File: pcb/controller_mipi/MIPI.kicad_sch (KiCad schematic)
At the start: 4 parts, among them J1 1-84952-5

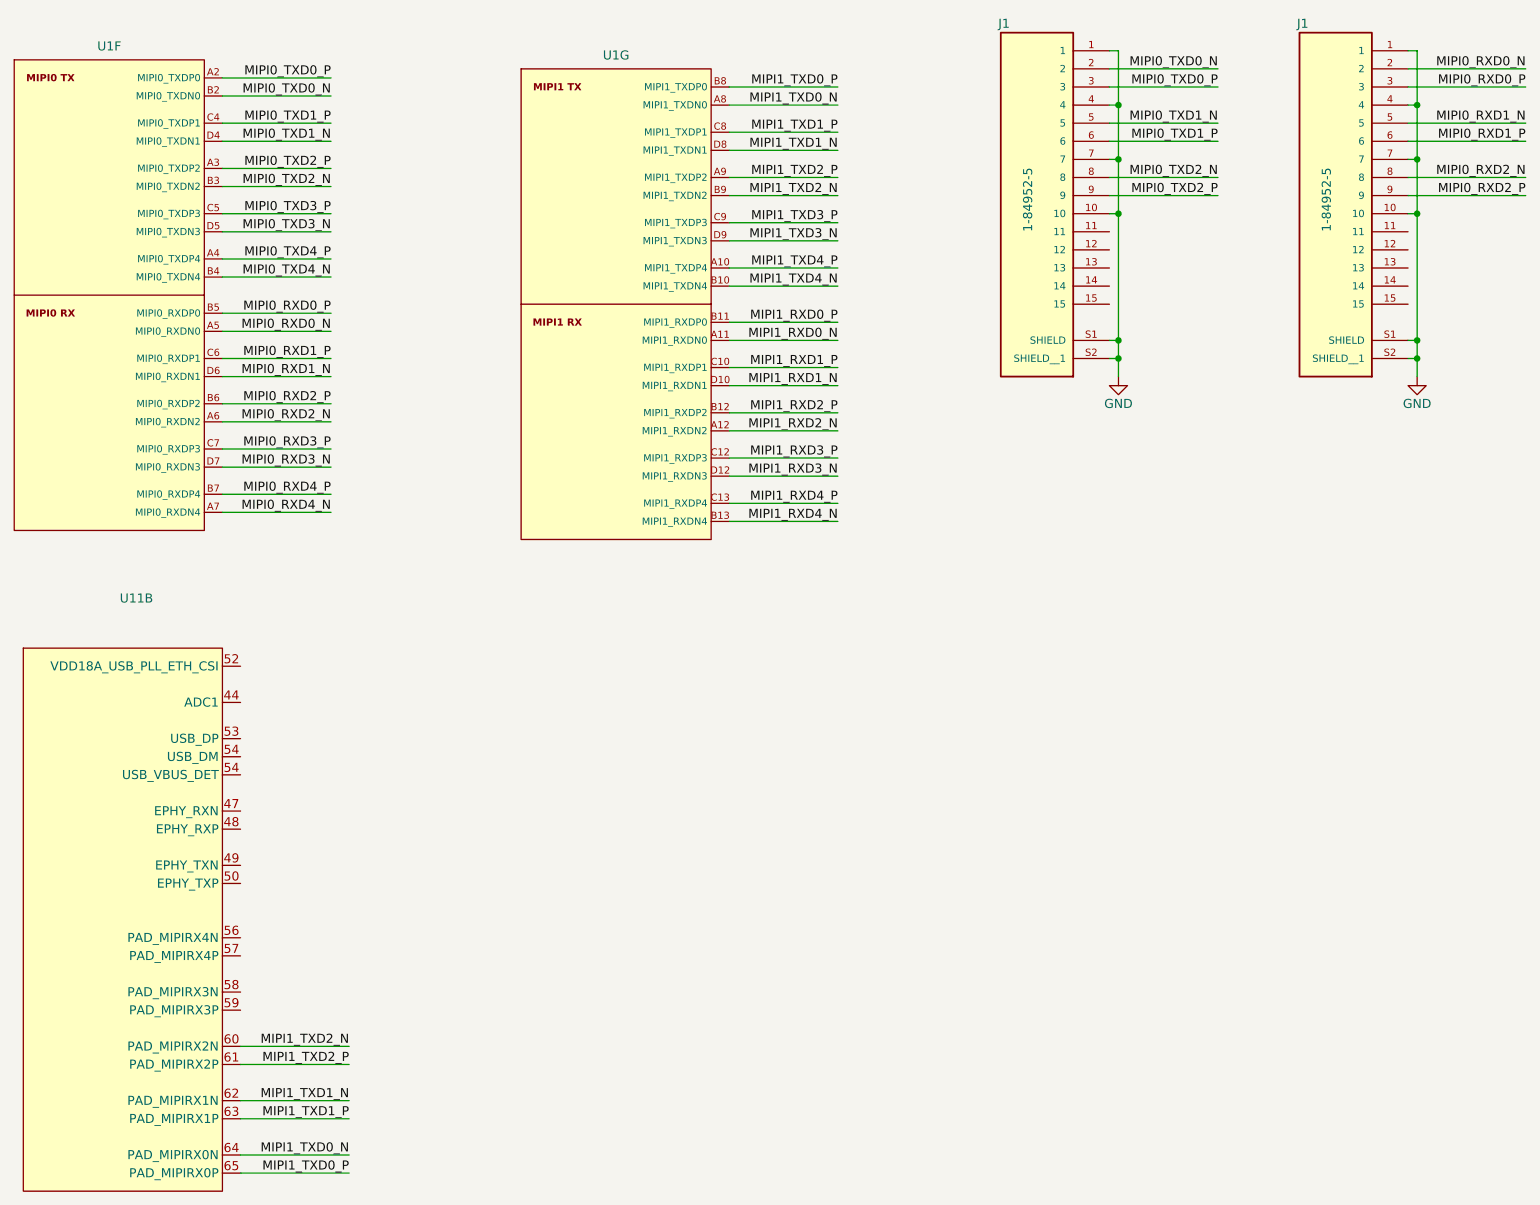
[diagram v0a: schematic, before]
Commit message: 4 mipi connectors exposed
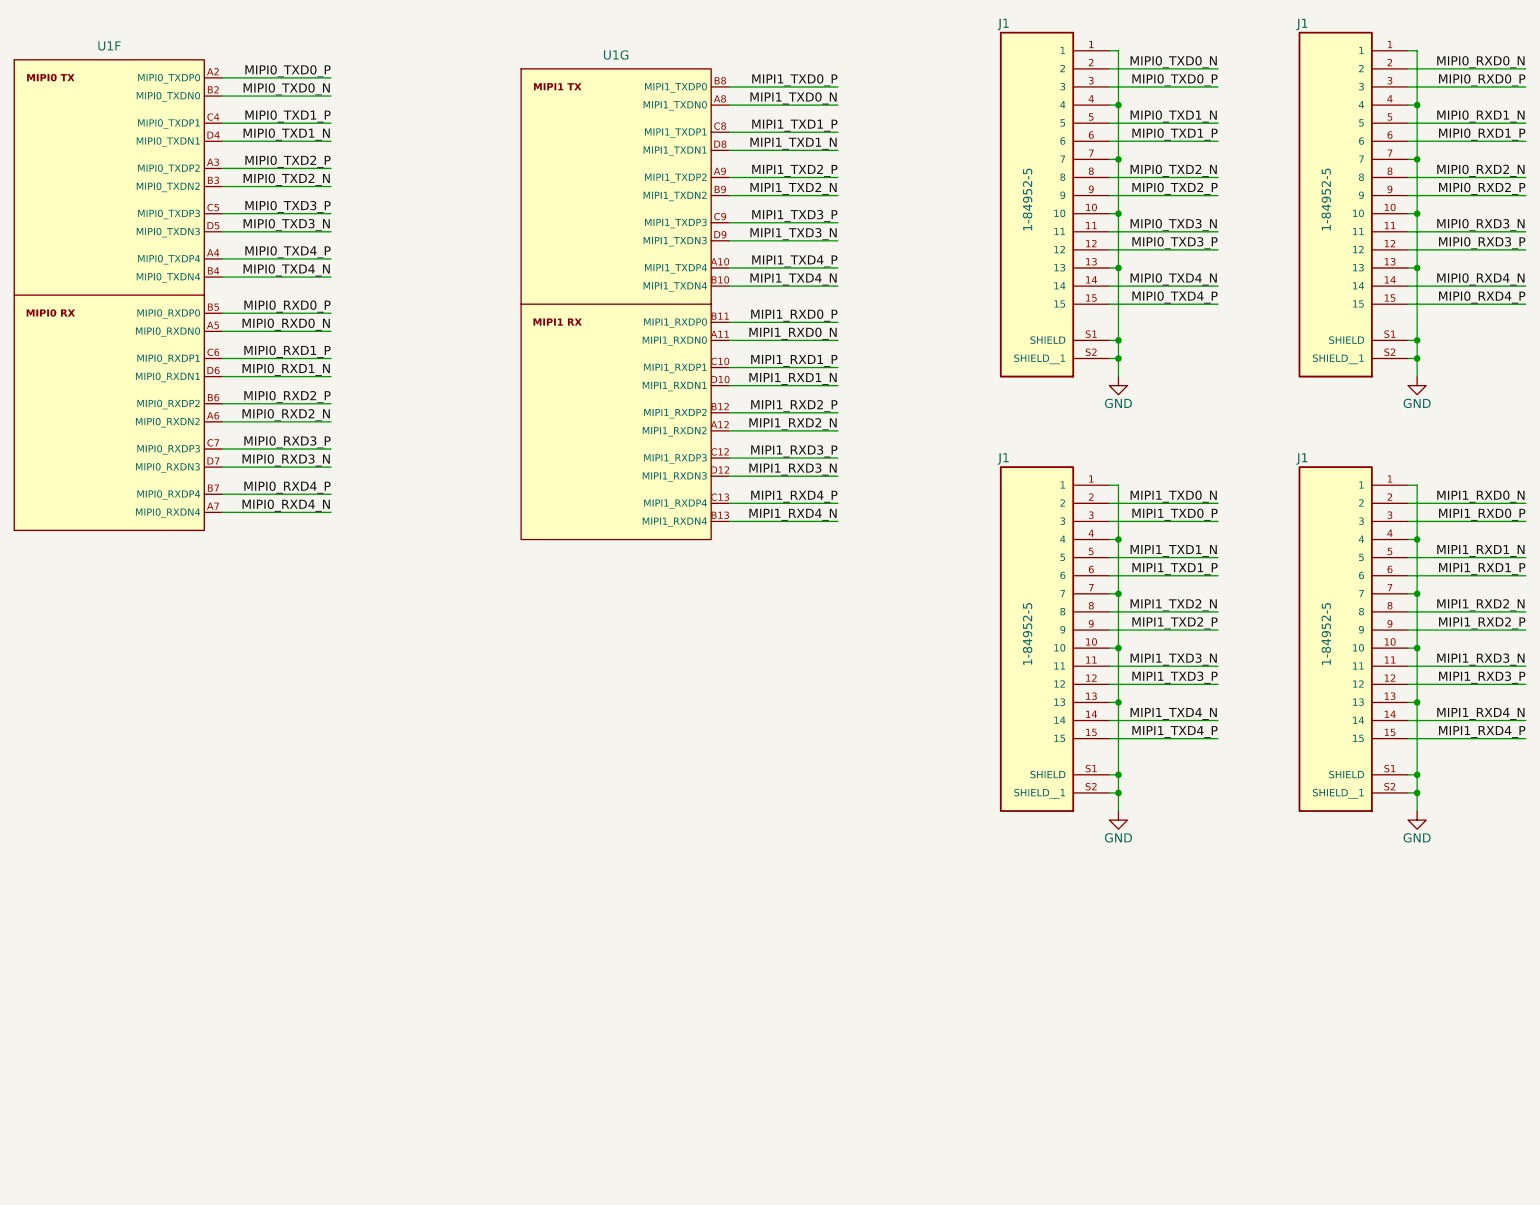
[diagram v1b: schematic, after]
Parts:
- removed U11: ~, smd:QFN-68_EP_7x7_Pitch0.35mm, symbol CVITEK:CV180xB
- added J1 (x2): 1-84952-5, smd:TE_1-84952-5, symbol 1-84952-5:1-84952-5
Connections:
- net GND: now also J1.13, J1.13, J1.1, J1.1, J1.10, J1.10, J1.13, J1.13, J1.4, J1.4, J1.7, J1.7, J1.S1 (SHIELD), J1.S1 (SHIELD), J1.S2 (SHIELD__1), J1.S2 (SHIELD__1)
- net MIPI0_RXD3_N: now also J1.11
- net MIPI0_RXD3_P: now also J1.12
- net MIPI0_RXD4_N: now also J1.14
- net MIPI0_RXD4_P: now also J1.15
- net MIPI0_TXD3_N: now also J1.11
- net MIPI0_TXD3_P: now also J1.12
- net MIPI0_TXD4_N: now also J1.14
- net MIPI0_TXD4_P: now also J1.15
- net MIPI1_RXD0_N: now also J1.2
- net MIPI1_RXD0_P: now also J1.3
- net MIPI1_RXD1_N: now also J1.5
- net MIPI1_RXD1_P: now also J1.6
- net MIPI1_RXD2_N: now also J1.8
- net MIPI1_RXD2_P: now also J1.9
- net MIPI1_RXD3_N: now also J1.11
- net MIPI1_RXD3_P: now also J1.12
- net MIPI1_RXD4_N: now also J1.14
- net MIPI1_RXD4_P: now also J1.15
- net MIPI1_TXD0_N: now also J1.2
- net MIPI1_TXD0_P: now also J1.3
- net MIPI1_TXD1_N: now also J1.5
- net MIPI1_TXD1_P: now also J1.6
- net MIPI1_TXD2_N: now also J1.8
- net MIPI1_TXD2_P: now also J1.9
- net MIPI1_TXD3_N: now also J1.11
- net MIPI1_TXD3_P: now also J1.12
- net MIPI1_TXD4_N: now also J1.14
- net MIPI1_TXD4_P: now also J1.15
